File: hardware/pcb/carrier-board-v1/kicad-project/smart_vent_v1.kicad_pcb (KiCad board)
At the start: 2 copper layers, 45 x 34 mm, 19 parts, among them J1 PinHeader_1x02_P2.54mm_Vertic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, J2 PinHeader_1x03_P2.54mm_Vertic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, Q1 SOT-23, Q2 SOT-23, SW1 SW_DIP_SPSTx01_Slide_9.78x4.7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, U1 PinHeader_1x07_P2.54mm_Vertic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

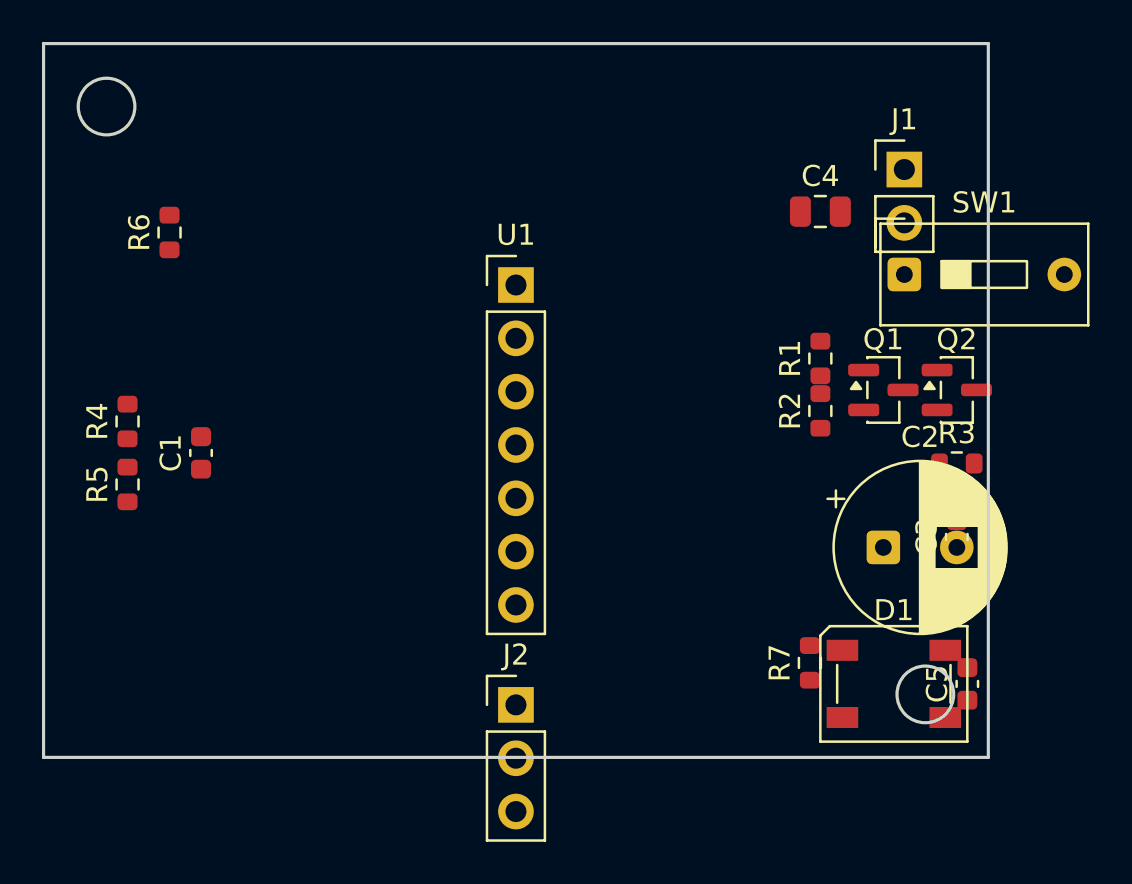
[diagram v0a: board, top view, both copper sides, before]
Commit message: Resolve all courtyard overlaps, shorts, and clearance violations in carrier board placement
DRC against real footprint sizes (issue #46) found the floorplan's
exact coordinates were sized around small SMD placeholders -- the
real stock substitutes for SW1 (THT slide switch, 10.37mm wide) and
C2 (THT radial cap, 8.59mm round) are much bigger, causing 3 shorts +
8 courtyard overlaps (with-LED) / 1 short + 5 overlaps (no-LED).

Adds nudge_apart.py, an iterative courtyard-separation solver, and
applies its resolved coordinates (plus one manual follow-up: J2's
last pad was landing past the board's bottom edge at its original
anchor, and separately collided with U1's placeholder footprint,
whose tall single-column shape doesn't represent the real XIAO
module) to build_board.py and place_smart_vent.py.

Re-running DRC on both variants: 0 shorts, 0 clearance violations,
0 courtyard overlaps, 0 board-edge clearance issues. Only cosmetic
silkscreen-text overlap remains. Regenerates the .kicad_pcb files
and the pipeline-validation Gerbers to match.
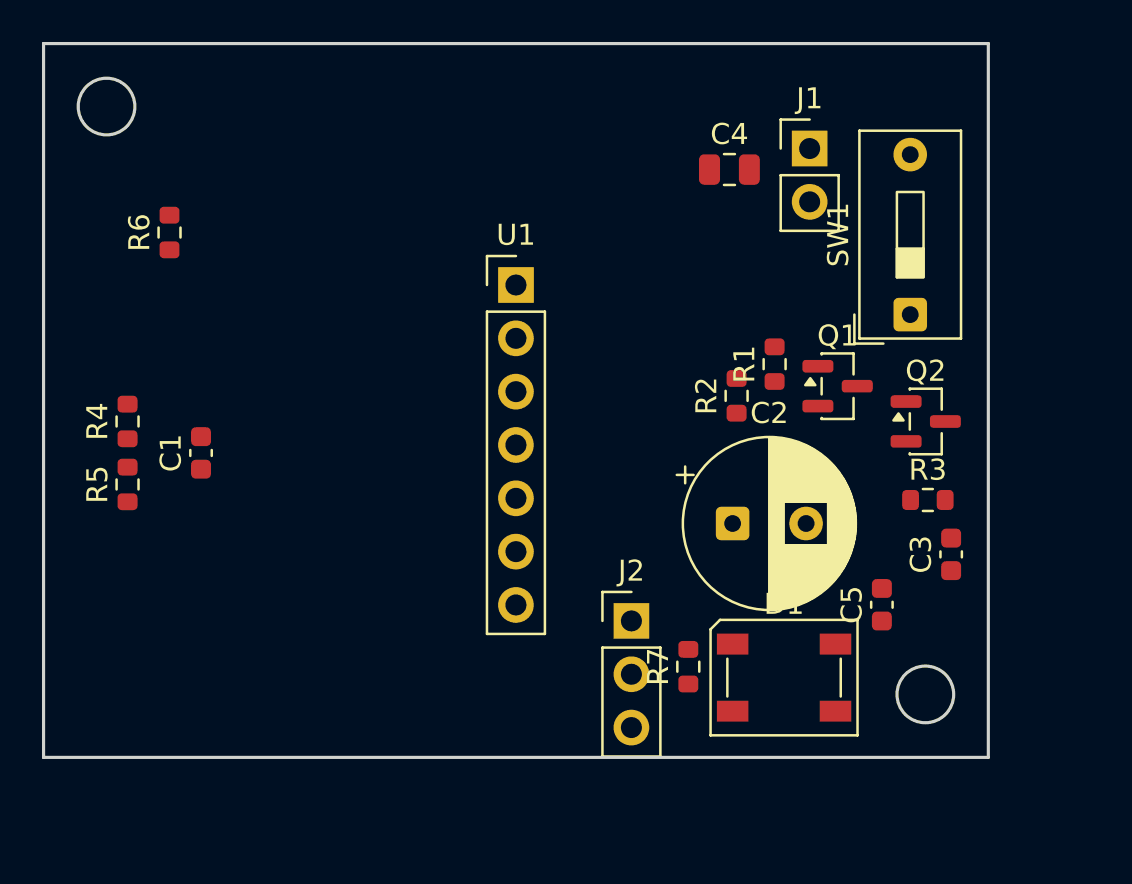
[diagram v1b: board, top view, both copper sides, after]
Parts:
- moved C2 7.27 mm to (62.8, 52.9)
- moved J2 6.80 mm to (58.0, 57.5)
- moved R7 5.79 mm to (60.7, 59.7)
- moved C5 5.55 mm to (69.9, 56.7)
- moved D1 5.24 mm to (65.3, 60.2)
- moved C4 4.77 mm to (62.7, 36.0)
- moved J1 4.62 mm to (66.5, 35.0)
- moved R2 4.05 mm to (63.0, 46.8)
- moved R3 2.22 mm to (72.1, 51.7)
- moved R1 2.20 mm to (64.8, 45.3)
- moved Q1 2.19 mm to (67.8, 46.3)
- moved Q2 2.11 mm to (72.0, 48.0)
- moved SW1 1.93 mm to (71.3, 42.9), turned to 90 degrees
- moved C3 0.87 mm to (73.2, 54.3)

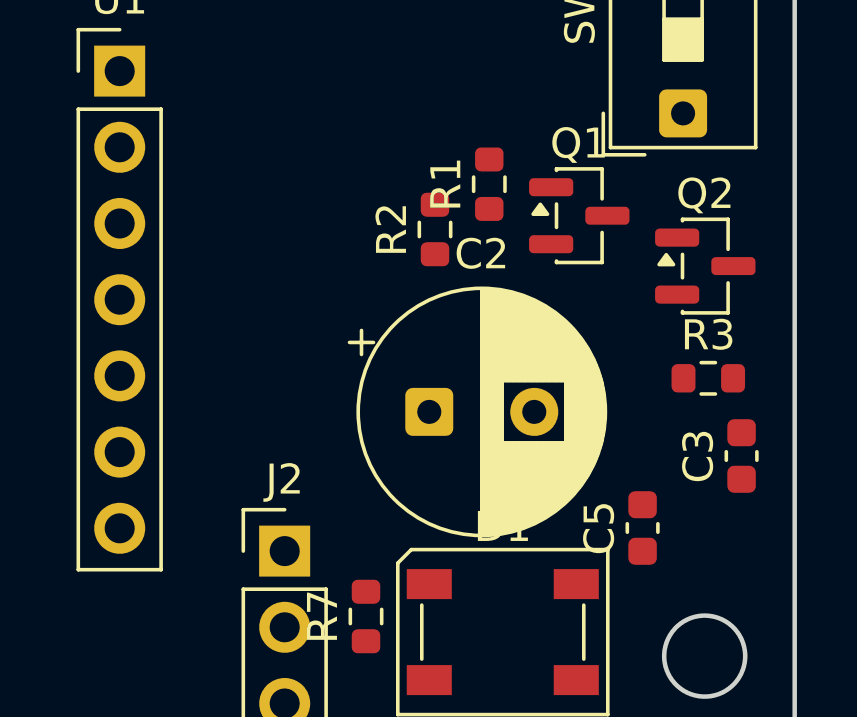
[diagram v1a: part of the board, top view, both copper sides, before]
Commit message: Resolve C2 footprint sourcing: Capacitor_SMD:CP_Elec_6.3x5.4 is in stock libs
The first placement pass searched only Capacitor_THT/Capacitor_Elec
libraries for C2's footprint and missed that the exact SMD part the
original netlist specified is filed under Capacitor_SMD.pretty. Swaps
it in for both variants in place of the bulkier THT radial stand-in,
narrowing issue #45 down to two remaining placeholders (U1, J1).

The real footprint's slightly different courtyard shape (9.69x7.19mm
vs the THT substitute's 8.59x8.59mm round) introduced one new minor
overlap with R2, fixed with a small nudge. DRC stays clean (0 shorts/
overlaps/clearance) on both variants after the fix.
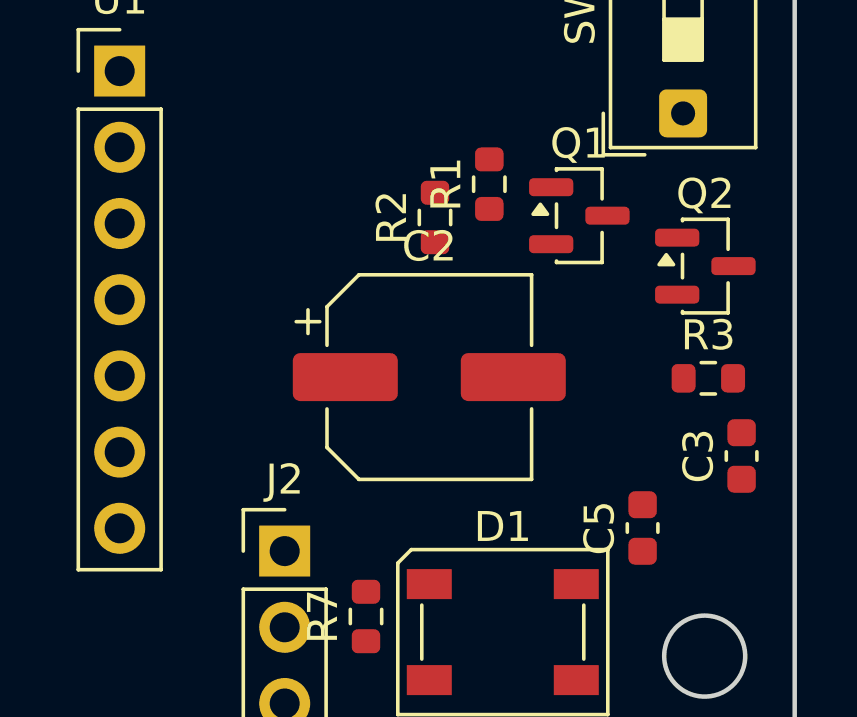
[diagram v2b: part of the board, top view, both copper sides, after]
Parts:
- C2: value CP_Radial_D8.0mm_P3.50mm -> CP_Elec_6.3x5.4; footprint CP_Radial_D8.0mm_P3.50mm -> CP_Elec_6.3x5.4
- moved C2 1.16 mm to (62.8, 51.7)
- moved R2 0.40 mm to (63.0, 46.4)
